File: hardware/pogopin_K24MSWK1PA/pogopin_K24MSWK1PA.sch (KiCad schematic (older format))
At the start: 6 parts

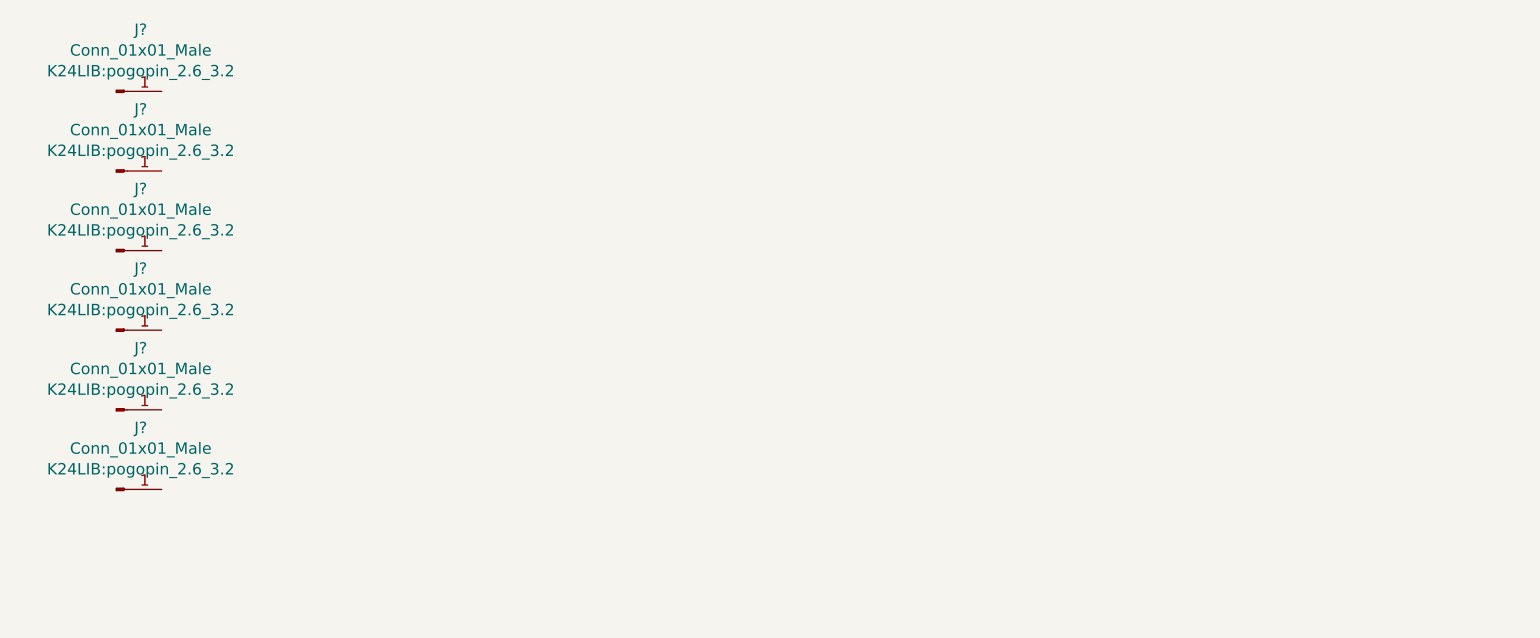
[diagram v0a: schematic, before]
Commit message: finished sch, started components layout
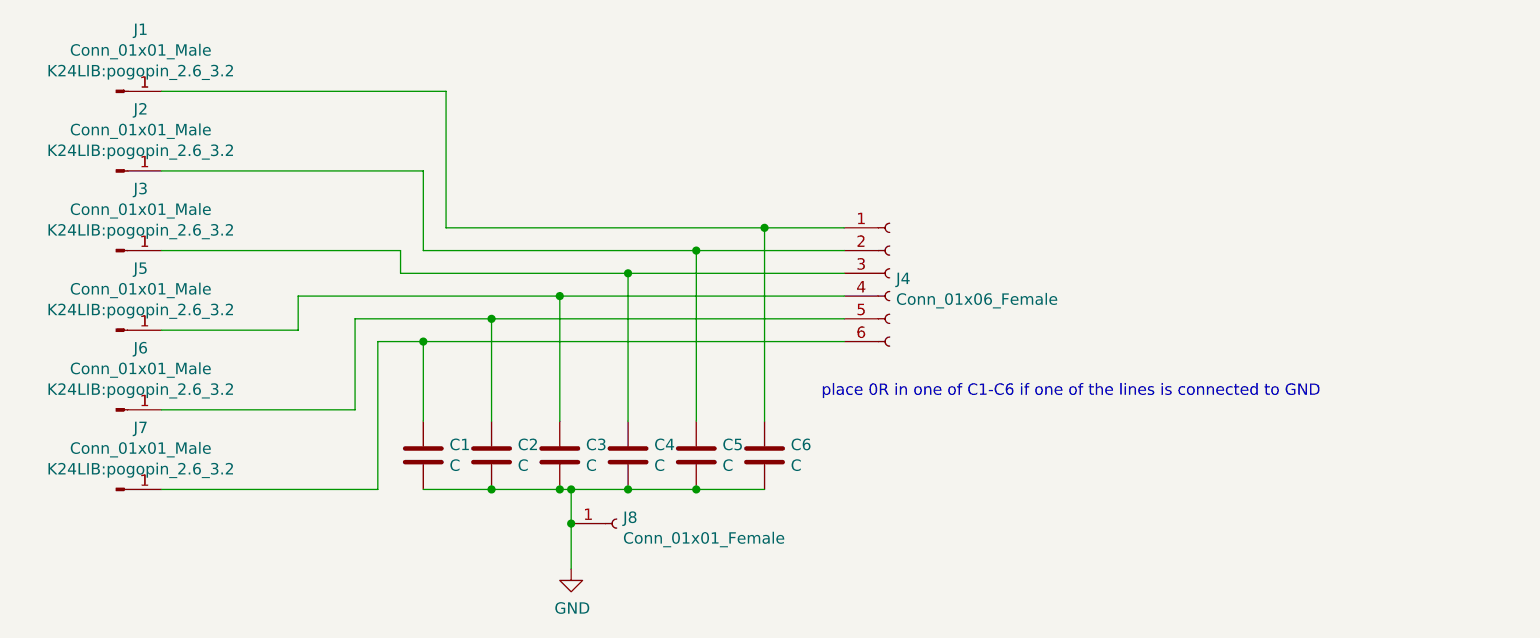
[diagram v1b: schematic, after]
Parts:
- added C1, C2, C3, C4, C5, C6: C, Capacitor_SMD:C_0805_2012Metric, symbol Device:C
- added J4: Conn_01x06_Female, Connector_JST:JST_PH_S6B-PH-K_1x06_P2.00mm_Horizontal, symbol Connector:Conn_01x06_Female
- added J8: Conn_01x01_Female, Connector_Wire:SolderWire-0.75sqmm_1x01_D1.25mm_OD3.5mm, symbol Connector:Conn_01x01_Female
- gave numbers to parts that had none: 6
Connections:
- net at J1.1 (Pin_1): now also C6.1, J4.1 (Pin_1)
- net at J2.1 (Pin_1): now also C5.1, J4.2 (Pin_2)
- net at J3.1 (Pin_1): now also C4.1, J4.3 (Pin_3)
- net at J5.1 (Pin_1): now also C3.1, J4.4 (Pin_4)
- net at J6.1 (Pin_1): now also C2.1, J4.5 (Pin_5)
- net at J7.1 (Pin_1): now also C1.1, J4.6 (Pin_6)
- new net GND: C1.2, C2.2, C3.2, C4.2, C5.2, C6.2, J8.1 (Pin_1)
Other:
- note added: "place 0R in one of C1-C6 if one of the lines is connected to GND\n"
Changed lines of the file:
@@
 $EndDescr
 $Comp
-L Connector:Conn_01x01_Male J?
+L Connector:Conn_01x01_Male J1
 U 1 1 65166475
 P 3400 2500
-F 0 "J?" H 3508 2771 50  0000 C CNN
+F 0 "J1" H 3508 2771 50  0000 C CNN
 F 1 "Conn_01x01_Male" H 3508 2680 50  0000 C CNN
 F 2 "K24LIB:pogopin_2.6_3.2" H 3508 2589 50  0000 C CNN
@@
 $EndComp
 $Comp
-L Connector:Conn_01x01_Male J?
+L Connector:Conn_01x01_Male J2
 U 1 1 65166CF1
 P 3400 2850
-F 0 "J?" H 3508 3121 50  0000 C CNN
+F 0 "J2" H 3508 3121 50  0000 C CNN
 F 1 "Conn_01x01_Male" H 3508 3030 50  0000 C CNN
 F 2 "K24LIB:pogopin_2.6_3.2" H 3508 2939 50  0000 C CNN
@@
 $EndComp
 $Comp
-L Connector:Conn_01x01_Male J?
+L Connector:Conn_01x01_Male J3
 U 1 1 6516714D
 P 3400 3200
-F 0 "J?" H 3508 3471 50  0000 C CNN
+F 0 "J3" H 3508 3471 50  0000 C CNN
 F 1 "Conn_01x01_Male" H 3508 3380 50  0000 C CNN
 F 2 "K24LIB:pogopin_2.6_3.2" H 3508 3289 50  0000 C CNN
@@
 $EndComp
 $Comp
-L Connector:Conn_01x01_Male J?
+L Connector:Conn_01x01_Male J5
 U 1 1 651674C6
 P 3400 3550
-F 0 "J?" H 3508 3821 50  0000 C CNN
+F 0 "J5" H 3508 3821 50  0000 C CNN
 F 1 "Conn_01x01_Male" H 3508 3730 50  0000 C CNN
 F 2 "K24LIB:pogopin_2.6_3.2" H 3508 3639 50  0000 C CNN
@@
 $EndComp
 $Comp
-L Connector:Conn_01x01_Male J?
+L Connector:Conn_01x01_Male J6
 U 1 1 651679E0
 P 3400 3900
-F 0 "J?" H 3508 4171 50  0000 C CNN
+F 0 "J6" H 3508 4171 50  0000 C CNN
 F 1 "Conn_01x01_Male" H 3508 4080 50  0000 C CNN
 F 2 "K24LIB:pogopin_2.6_3.2" H 3508 3989 50  0000 C CNN
@@
 $EndComp
 $Comp
-L Connector:Conn_01x01_Male J?
+L Connector:Conn_01x01_Male J7
 U 1 1 65167EDD
 P 3400 4250
-F 0 "J?" H 3508 4521 50  0000 C CNN
+F 0 "J7" H 3508 4521 50  0000 C CNN
 F 1 "Conn_01x01_Male" H 3508 4430 50  0000 C CNN
 F 2 "K24LIB:pogopin_2.6_3.2" H 3508 4339 50  0000 C CNN
@@
 	1    0    0    -1
 $EndComp
+$Comp
+L Connector:Conn_01x06_Female J4
+U 1 1 65182A6F
+P 6800 3300
+F 0 "J4" H 6828 3276 50  0000 L CNN
+F 1 "Conn_01x06_Female" H 6828 3185 50  0000 L CNN
+F 2 "Connector_JST:JST_PH_S6B-PH-K_1x06_P2.00mm_Horizontal" H 6800 3300 50  0001 C CNN
+F 3 "~" H 6800 3300 50  0001 C CNN
+	1    6800 3300
+	1    0    0    -1
+$EndComp
+Wire Wire Line
+	3600 2500 4850 2500
+Wire Wire Line
+	4850 2500 4850 3100
+Wire Wire Line
+	4850 3100 6250 3100
+Wire Wire Line
+	6600 3200 5950 3200
+Wire Wire Line
+	4750 3200 4750 2850
+Wire Wire Line
+	4750 2850 3600 2850
+Wire Wire Line
+	6600 3300 5650 3300
+Wire Wire Line
+	4650 3300 4650 3200
+Wire Wire Line
+	4650 3200 3600 3200
+Wire Wire Line
+	6600 3400 5350 3400
+Wire Wire Line
+	4200 3400 4200 3550
+Wire Wire Line
+	4200 3550 3600 3550
+Wire Wire Line
+	4450 3500 4450 3900
+Wire Wire Line
+	4450 3900 3600 3900
+Wire Wire Line
+	6600 3600 4750 3600
+Wire Wire Line
+	4550 3600 4550 4250
+Wire Wire Line
+	4550 4250 3600 4250
+Wire Wire Line
+	4450 3500 5050 3500
+$Comp
+L Device:C C1
+U 1 1 65185742
+P 4750 4100
+F 0 "C1" H 4865 4146 50  0000 L CNN
+F 1 "C" H 4865 4055 50  0000 L CNN
+F 2 "Capacitor_SMD:C_0805_2012Metric" H 4788 3950 50  0001 C CNN
+F 3 "~" H 4750 4100 50  0001 C CNN
+	1    4750 4100
+	1    0    0    -1
+$EndComp
+Wire Wire Line
+	4750 3950 4750 3600
+Connection ~ 4750 3600
+Wire Wire Line
+	4750 3600 4550 3600
+Wire Wire Line
+	5050 3950 5050 3500
+Connection ~ 5050 3500
+Wire Wire Line
+	5050 3500 6600 3500
+Wire Wire Line
+	5350 3950 5350 3400
+Connection ~ 5350 3400
+Wire Wire Line
+	5350 3400 4200 3400
+Wire Wire Line
+	5650 3950 5650 3300
+Connection ~ 5650 3300
+Wire Wire Line
+	5650 3300 4650 3300
+Wire Wire Line
+	5950 3950 5950 3200
+Connection ~ 5950 3200
+Wire Wire Line
+	5950 3200 4750 3200
+Wire Wire Line
+	6250 3950 6250 3100
+Connection ~ 6250 3100
+Wire Wire Line
+	6250 3100 6600 3100
+$Comp
+L power:GND #PWR01
+U 1 1 6518C973
+P 5400 4600
+F 0 "#PWR01" H 5400 4350 50  0001 C CNN
+F 1 "GND" H 5405 4427 50  0000 C CNN
+F 2 "" H 5400 4600 50  0001 C CNN
+F 3 "" H 5400 4600 50  0001 C CNN
+	1    5400 4600
+	1    0    0    -1
+$EndComp
+Wire Wire Line
+	5400 4600 5400 4400
+Connection ~ 5400 4250
+$Comp
+L Connector:Conn_01x01_Female J8
+U 1 1 6518E052
+P 5600 4400
+F 0 "J8" H 5628 4426 50  0000 L CNN
+F 1 "Conn_01x01_Female" H 5628 4335 50  0000 L CNN
+F 2 "Connector_Wire:SolderWire-0.75sqmm_1x01_D1.25mm_OD3.5mm" H 5600 4400 50  0001 C CNN
+F 3 "~" H 5600 4400 50  0001 C CNN
+	1    5600 4400
+	1    0    0    -1
+$EndComp
+Connection ~ 5400 4400
+Wire Wire Line
+	5400 4400 5400 4250
+Wire Wire Line
+	4750 4250 5050 4250
+Wire Wire Line
+	5400 4250 5650 4250
+$Comp
+L Device:C C2
+U 1 1 6518E8F0
+P 5050 4100
+F 0 "C2" H 5165 4146 50  0000 L CNN
+F 1 "C" H 5165 4055 50  0000 L CNN
+F 2 "Capacitor_SMD:C_0805_2012Metric" H 5088 3950 50  0001 C CNN
+F 3 "~" H 5050 4100 50  0001 C CNN
+	1    5050 4100
+	1    0    0    -1
+$EndComp
+Connection ~ 5050 4250
+Wire Wire Line
+	5050 4250 5350 4250
+$Comp
+L Device:C C3
+U 1 1 6518ED40
+P 5350 4100
+F 0 "C3" H 5465 4146 50  0000 L CNN
+F 1 "C" H 5465 4055 50  0000 L CNN
+F 2 "Capacitor_SMD:C_0805_2012Metric" H 5388 3950 50  0001 C CNN
+F 3 "~" H 5350 4100 50  0001 C CNN
+	1    5350 4100
+	1    0    0    -1
+$EndComp
+Connection ~ 5350 4250
+Wire Wire Line
+	5350 4250 5400 4250
+$Comp
+L Device:C C4
+U 1 1 6518F090
+P 5650 4100
+F 0 "C4" H 5765 4146 50  0000 L CNN
+F 1 "C" H 5765 4055 50  0000 L CNN
+F 2 "Capacitor_SMD:C_0805_2012Metric" H 5688 3950 50  0001 C CNN
+F 3 "~" H 5650 4100 50  0001 C CNN
+	1    5650 4100
+	1    0    0    -1
+$EndComp
+Connection ~ 5650 4250
+Wire Wire Line
+	5650 4250 5950 4250
+$Comp
+L Device:C C5
+U 1 1 6518F361
+P 5950 4100
+F 0 "C5" H 6065 4146 50  0000 L CNN
+F 1 "C" H 6065 4055 50  0000 L CNN
+F 2 "Capacitor_SMD:C_0805_2012Metric" H 5988 3950 50  0001 C CNN
+F 3 "~" H 5950 4100 50  0001 C CNN
+	1    5950 4100
+	1    0    0    -1
+$EndComp
+Connection ~ 5950 4250
+Wire Wire Line
+	5950 4250 6250 4250
+$Comp
+L Device:C C6
+U 1 1 6518F5E6
+P 6250 4100
+F 0 "C6" H 6365 4146 50  0000 L CNN
+F 1 "C" H 6365 4055 50  0000 L CNN
+F 2 "Capacitor_SMD:C_0805_2012Metric" H 6288 3950 50  0001 C CNN
+F 3 "~" H 6250 4100 50  0001 C CNN
+	1    6250 4100
+	1    0    0    -1
+$EndComp
+Text Notes 6500 3850 0    50   ~ 0
+place 0R in one of C1-C6 if one of the lines is connected to GND\n
 $EndSCHEMATC
